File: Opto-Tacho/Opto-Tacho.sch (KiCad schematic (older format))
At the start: 1 part, among them J101 Interface

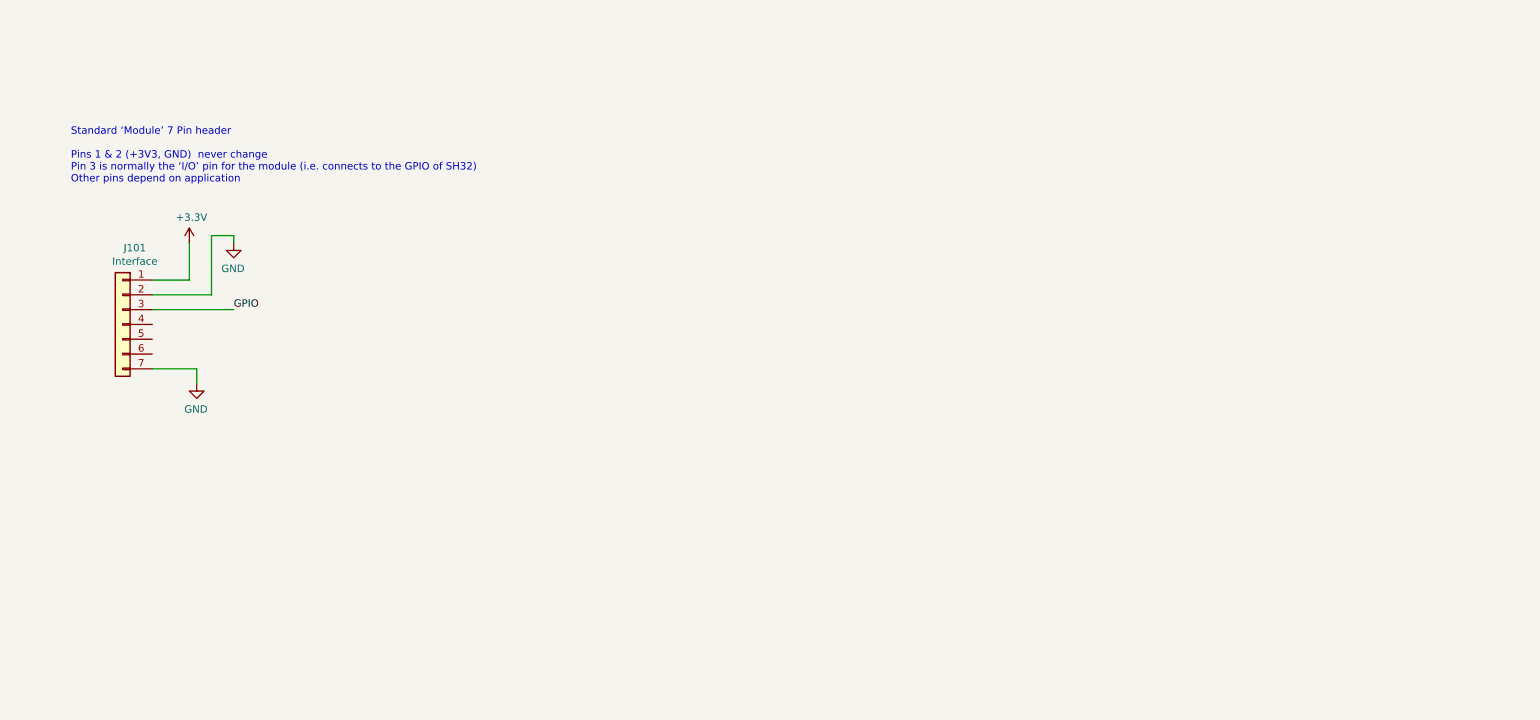
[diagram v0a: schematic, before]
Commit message: Opto Tacho (Schmidtt),   Fixes to FET_Driver_Sense
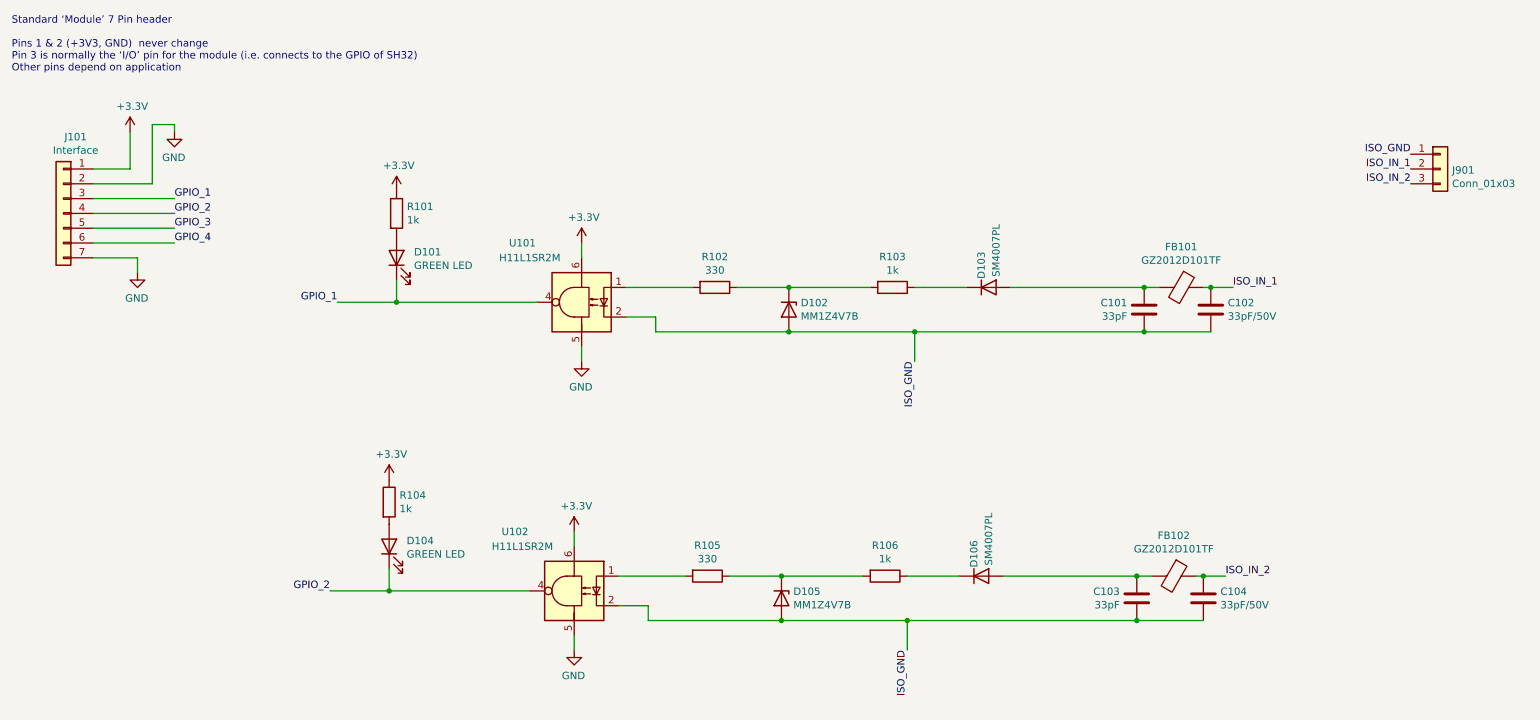
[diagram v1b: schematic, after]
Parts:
- added C101, C103: 33pF, Capacitor_SMD:C_0402_1005Metric, symbol Device:C
- added C102, C104: 33pF/50V, Capacitor_SMD:C_0603_1608Metric, symbol Device:C
- added D101, D104: GREEN LED, LED_SMD:LED_0603_1608Metric, symbol Device:LED
- added D102, D105: MM1Z4V7B, Diode_SMD:D_SOD-123, symbol Diode:BZT52Bxx
- added D103, D106: SM4007PL, Diode_SMD:D_SOD-123F, symbol Device:D
- added FB102, FB903: GZ2012D101TF, Inductor_SMD:L_0805_2012Metric, symbol Device:Ferrite_Bead
- added J901: Conn_01x03, Connector_PinHeader_2.54mm:PinHeader_1x03_P2.54mm_Vertical, symbol Connector_Generic:Conn_01x03
- added R101, R104: 1k, Resistor_SMD:R_0402_1005Metric, symbol Device:R
- added R102, R105: 330, Resistor_SMD:R_0603_1608Metric, symbol Device:R
- added R103, R106: 1k, Resistor_SMD:R_0603_1608Metric, symbol Device:R
- added U101, U102: H11L1SR2M, yacht_hardware:SMT-6_6.4x8.5x2.54P, symbol Isolator:H11L1
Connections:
- net +3V3: now also R101.1, R104.1, U101.6, U102.6
- net GND: now also U101.5, U102.5
- net GPIO_2: now reaches J101.4 (Pin_4)
- net GPIO_2: now also D104.1 (K), U102.4
- net GPIO_3: now reaches J101.5 (Pin_5)
- net GPIO_4: now reaches J101.6 (Pin_6)
- net GPIO renamed GPIO_1
- net GPIO_1: now also D101.1 (K), U101.4
- new net: D102.1 (K), R102.1, R103.2
- new net: R102.2, U101.1
- new net: C101.1, D103.2 (A), FB903.2
- new net: D103.1 (K), R103.1
- new net: C103.1, D106.2 (A), FB102.2
- new net: D105.1 (K), R105.1, R106.2
- new net: R105.2, U102.1
- new net: D106.1 (K), R106.1
- new net: D104.2 (A), R104.2
- new net: D101.2 (A), R101.2
- new net ISO_GND: C101.2, C102.2, C103.2, C104.2, D102.2 (A), D105.2 (A), J901.1 (Pin_1), U101.2, U102.2
- new net ISO_IN_1: C102.1, FB903.1, J901.2 (Pin_2)
- new net ISO_IN_2: C104.1, FB102.1, J901.3 (Pin_3)
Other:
- moved on the sheet: J101

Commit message: Production Tidyup - LCSC Part Numbers
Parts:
- R101, R104: LCSC (none) -> C11702
- R102, R105: LCSC (none) -> C23138
- R103, R106: LCSC (none) -> C21190
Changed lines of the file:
@@
 F 2 "Resistor_SMD:R_0603_1608Metric" V 5330 2450 50  0001 C CNN
 F 3 "~" H 5400 2450 50  0001 C CNN
-F 4 "" H 5400 2450 50  0001 C CNN "LCSC"
+F 4 "C23138" H 5400 2450 50  0001 C CNN "LCSC"
 	1    5400 2450
 	0    1    1    0
@@
 F 2 "Resistor_SMD:R_0603_1608Metric" V 6530 2450 50  0001 C CNN
 F 3 "~" H 6600 2450 50  0001 C CNN
-F 4 "" H 6600 2450 50  0001 C CNN "LCSC"
+F 4 "C21190" H 6600 2450 50  0001 C CNN "LCSC"
 	1    6600 2450
 	0    1    1    0
@@
 F 2 "Resistor_SMD:R_0402_1005Metric" V 3180 1950 50  0001 C CNN
 F 3 "~" H 3250 1950 50  0001 C CNN
-F 4 "" H 3250 1950 50  0001 C CNN "LCSC"
+F 4 "C11702" H 3250 1950 50  0001 C CNN "LCSC"
 	1    3250 1950
 	1    0    0    -1
@@
 F 2 "Resistor_SMD:R_0603_1608Metric" V 5280 4400 50  0001 C CNN
 F 3 "~" H 5350 4400 50  0001 C CNN
-F 4 "" H 5350 4400 50  0001 C CNN "LCSC"
+F 4 "C23138" H 5350 4400 50  0001 C CNN "LCSC"
 	1    5350 4400
 	0    1    1    0
@@
 F 2 "Resistor_SMD:R_0603_1608Metric" V 6480 4400 50  0001 C CNN
 F 3 "~" H 6550 4400 50  0001 C CNN
-F 4 "" H 6550 4400 50  0001 C CNN "LCSC"
+F 4 "C21190" H 6550 4400 50  0001 C CNN "LCSC"
 	1    6550 4400
 	0    1    1    0
@@
 F 2 "Resistor_SMD:R_0402_1005Metric" V 3130 3900 50  0001 C CNN
 F 3 "~" H 3200 3900 50  0001 C CNN
-F 4 "" H 3200 3900 50  0001 C CNN "LCSC"
+F 4 "C11702" H 3200 3900 50  0001 C CNN "LCSC"
 	1    3200 3900
 	1    0    0    -1

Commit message: Fix Resistor sizes to all are 603
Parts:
- R101, R104: footprint Resistor_SMD:R_0402_1005Metric -> Resistor_SMD:R_0603_1608Metric; LCSC C11702 -> C21190
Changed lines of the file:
@@
 F 0 "R101" H 3320 1996 50  0000 L CNN
 F 1 "1k" H 3320 1905 50  0000 L CNN
-F 2 "Resistor_SMD:R_0402_1005Metric" V 3180 1950 50  0001 C CNN
+F 2 "Resistor_SMD:R_0603_1608Metric" V 3180 1950 50  0001 C CNN
 F 3 "~" H 3250 1950 50  0001 C CNN
-F 4 "C11702" H 3250 1950 50  0001 C CNN "LCSC"
+F 4 "C21190" H 3250 1950 50  0001 C CNN "LCSC"
 	1    3250 1950
 	1    0    0    -1
@@
 F 0 "R104" H 3270 3946 50  0000 L CNN
 F 1 "1k" H 3270 3855 50  0000 L CNN
-F 2 "Resistor_SMD:R_0402_1005Metric" V 3130 3900 50  0001 C CNN
+F 2 "Resistor_SMD:R_0603_1608Metric" V 3130 3900 50  0001 C CNN
 F 3 "~" H 3200 3900 50  0001 C CNN
-F 4 "C11702" H 3200 3900 50  0001 C CNN "LCSC"
+F 4 "C21190" H 3200 3900 50  0001 C CNN "LCSC"
 	1    3200 3900
 	1    0    0    -1
